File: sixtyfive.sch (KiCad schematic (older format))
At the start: 169 parts, among them J1 Conn_01x12, J2 Conn_ARM_JTAG_SWD_10, Q1 BSS138, SW1 SW_Push, U1 SRV05-4, U2 STM32F072C8Tx, U3 MCP1700-3302E_SOT23

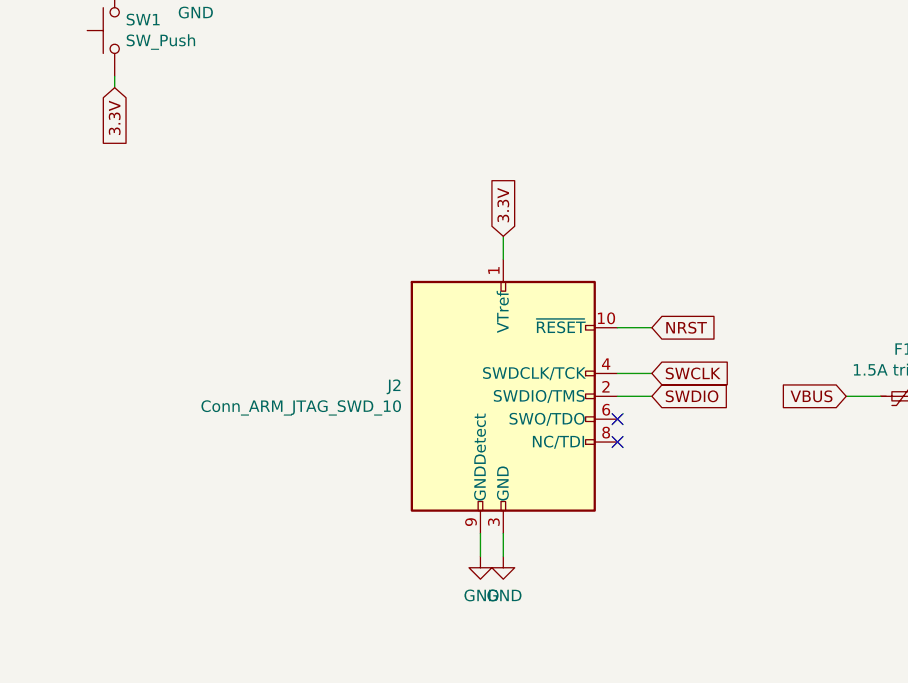
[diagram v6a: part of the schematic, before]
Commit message: Added some decoration, changed the connector and rerouted a tiny bit
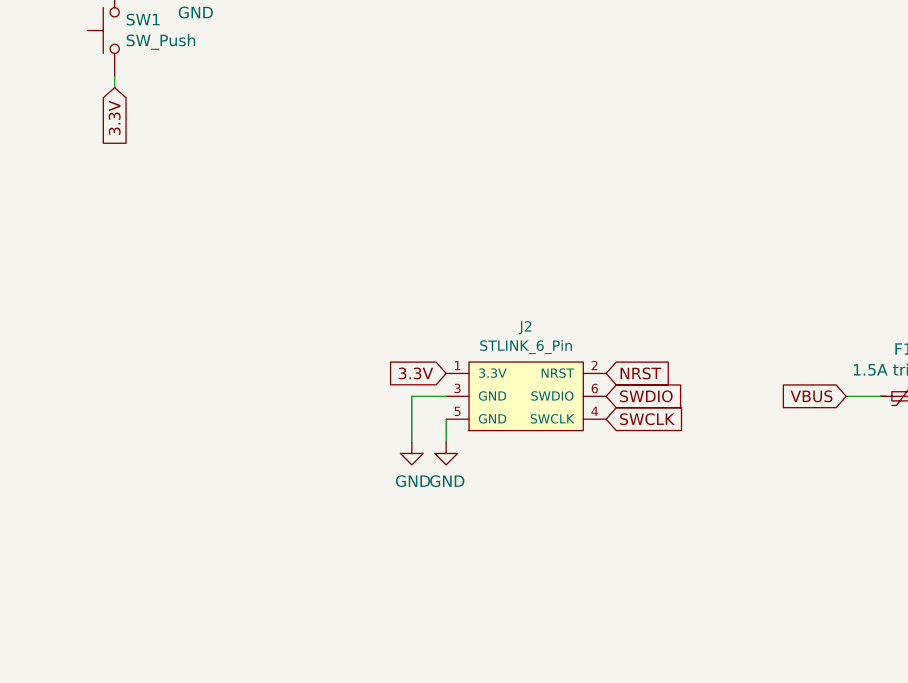
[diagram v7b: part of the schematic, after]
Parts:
- removed J2: Conn_ARM_JTAG_SWD_10, sixtyfive:Conn_ARM_JTAG_SWD_10, symbol Connector:Conn_ARM_JTAG_SWD_10
- added J2: STLINK_6_Pin, 2X3_LOCK, symbol SparkFun-Connectors:STLINK_6_Pin
- DF1: footprint Diode_SMD:D_SOD-123 -> Diode_SMD:D_SMB
- DRGB1, DRGB10, DRGB2, DRGB3, DRGB4, DRGB5, DRGB6, DRGB7, DRGB8, DRGB9: JLCCode (none) -> C114586
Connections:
- net 3.3V: now also J2.1 (3.3V)
- net GND: now also J2.3 (GND), J2.5 (GND)
- net NRST: now also J2.2 (NRST)
- net SWCLK: now also J2.4 (SWCLK)
- net SWDIO: now also J2.6 (SWDIO)
- no-connect marks 6 -> 4
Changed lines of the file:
@@
 Text GLabel 30350 10350 1    50   Input ~ 0
 Col14
-$Comp
-L Connector:Conn_ARM_JTAG_SWD_10 J2
-U 1 1 5F4F806F
-P 22000 20850
-F 0 "J2" H 21557 20896 50  0000 R CNN
-F 1 "Conn_ARM_JTAG_SWD_10" H 21557 20805 50  0000 R CNN
-F 2 "sixtyfive:Conn_ARM_JTAG_SWD_10" H 22000 20850 50  0001 C CNN
-F 3 "http://infocenter.arm.com/help/topic/com.arm.doc.ddi0314h/DDI0314H_coresight_components_trm.pdf" V 21650 19600 50  0001 C CNN
-	1    22000 20850
-	1    0    0    -1
-$EndComp
-Text GLabel 22000 20150 1    50   Input ~ 0
+Text GLabel 21750 20750 0    50   Input ~ 0
 3.3V
-Wire Wire Line
-	22000 20150 22000 20250
 $Comp
 L power:GND #PWR0114
 U 1 1 5F517BF8
-P 21900 21550
-F 0 "#PWR0114" H 21900 21300 50  0001 C CNN
-F 1 "GND" H 21905 21377 50  0000 C CNN
-F 2 "" H 21900 21550 50  0001 C CNN
-F 3 "" H 21900 21550 50  0001 C CNN
-	1    21900 21550
+P 21750 21050
+F 0 "#PWR0114" H 21750 20800 50  0001 C CNN
+F 1 "GND" H 21755 20877 50  0000 C CNN
+F 2 "" H 21750 21050 50  0001 C CNN
+F 3 "" H 21750 21050 50  0001 C CNN
+	1    21750 21050
 	1    0    0    -1
 $EndComp
@@
 L power:GND #PWR0115
 U 1 1 5F519B31
-P 22000 21550
-F 0 "#PWR0115" H 22000 21300 50  0001 C CNN
-F 1 "GND" H 22005 21377 50  0000 C CNN
-F 2 "" H 22000 21550 50  0001 C CNN
-F 3 "" H 22000 21550 50  0001 C CNN
-	1    22000 21550
-	1    0    0    -1
-$EndComp
-Wire Wire Line
-	22000 21550 22000 21450
-Wire Wire Line
-	21900 21450 21900 21550
-Text GLabel 22650 20550 2    50   Input ~ 0
+P 21600 21050
+F 0 "#PWR0115" H 21600 20800 50  0001 C CNN
+F 1 "GND" H 21605 20877 50  0000 C CNN
+F 2 "" H 21600 21050 50  0001 C CNN
+F 3 "" H 21600 21050 50  0001 C CNN
+	1    21600 21050
+	1    0    0    -1
+$EndComp
+Text GLabel 22450 20750 2    50   Input ~ 0
 NRST
-Text GLabel 22650 20750 2    50   Input ~ 0
+Text GLabel 22450 20950 2    50   Input ~ 0
 SWCLK
-Text GLabel 22650 20850 2    50   Input ~ 0
+Text GLabel 22450 20850 2    50   Input ~ 0
 SWDIO
-Wire Wire Line
-	22650 20850 22500 20850
-Wire Wire Line
-	22500 20750 22650 20750
-Wire Wire Line
-	22650 20550 22500 20550
-NoConn ~ 22500 20950
-NoConn ~ 22500 21050
 Text GLabel 29650 18600 2    50   Input ~ 0
 SWDIO
@@
 F 2 "LED_SMD:LED_WS2812B_PLCC4_5.0x5.0mm_P3.2mm" H 11950 18800 50  0001 L TNN
 F 3 "https://cdn-shop.adafruit.com/datasheets/WS2812B.pdf" H 12000 18725 50  0001 L TNN
+F 4 "C114586" H 8300 19100 50  0001 C CNN "JLCCode"
 	1    11900 19100
 	1    0    0    -1
@@
 F 2 "LED_SMD:LED_WS2812B_PLCC4_5.0x5.0mm_P3.2mm" H 12850 18800 50  0001 L TNN
 F 3 "https://cdn-shop.adafruit.com/datasheets/WS2812B.pdf" H 12900 18725 50  0001 L TNN
+F 4 "C114586" H 8300 19100 50  0001 C CNN "JLCCode"
 	1    12800 19100
 	1    0    0    -1
@@
 F 2 "LED_SMD:LED_WS2812B_PLCC4_5.0x5.0mm_P3.2mm" H 13750 18800 50  0001 L TNN
 F 3 "https://cdn-shop.adafruit.com/datasheets/WS2812B.pdf" H 13800 18725 50  0001 L TNN
+F 4 "C114586" H 8300 19100 50  0001 C CNN "JLCCode"
 	1    13700 19100
 	1    0    0    -1
@@
 F 2 "LED_SMD:LED_WS2812B_PLCC4_5.0x5.0mm_P3.2mm" H 14650 18800 50  0001 L TNN
 F 3 "https://cdn-shop.adafruit.com/datasheets/WS2812B.pdf" H 14700 18725 50  0001 L TNN
+F 4 "C114586" H 8300 19100 50  0001 C CNN "JLCCode"
 	1    14600 19100
 	1    0    0    -1
@@
 F 2 "LED_SMD:LED_WS2812B_PLCC4_5.0x5.0mm_P3.2mm" H 8350 18800 50  0001 L TNN
 F 3 "https://cdn-shop.adafruit.com/datasheets/WS2812B.pdf" H 8400 18725 50  0001 L TNN
+F 4 "C114586" H 8300 19100 50  0001 C CNN "JLCCode"
 	1    8300 19100
 	1    0    0    -1
@@
 F 2 "LED_SMD:LED_WS2812B_PLCC4_5.0x5.0mm_P3.2mm" H 9250 18800 50  0001 L TNN
 F 3 "https://cdn-shop.adafruit.com/datasheets/WS2812B.pdf" H 9300 18725 50  0001 L TNN
+F 4 "C114586" H 8300 19100 50  0001 C CNN "JLCCode"
 	1    9200 19100
 	1    0    0    -1
@@
 F 2 "LED_SMD:LED_WS2812B_PLCC4_5.0x5.0mm_P3.2mm" H 10150 18800 50  0001 L TNN
 F 3 "https://cdn-shop.adafruit.com/datasheets/WS2812B.pdf" H 10200 18725 50  0001 L TNN
+F 4 "C114586" H 8300 19100 50  0001 C CNN "JLCCode"
 	1    10100 19100
 	1    0    0    -1
@@
 F 2 "LED_SMD:LED_WS2812B_PLCC4_5.0x5.0mm_P3.2mm" H 11050 18800 50  0001 L TNN
 F 3 "https://cdn-shop.adafruit.com/datasheets/WS2812B.pdf" H 11100 18725 50  0001 L TNN
+F 4 "C114586" H 8300 19100 50  0001 C CNN "JLCCode"
 	1    11000 19100
 	1    0    0    -1
@@
 F 2 "LED_SMD:LED_WS2812B_PLCC4_5.0x5.0mm_P3.2mm" H 15550 18800 50  0001 L TNN
 F 3 "https://cdn-shop.adafruit.com/datasheets/WS2812B.pdf" H 15600 18725 50  0001 L TNN
+F 4 "C114586" H 8300 19100 50  0001 C CNN "JLCCode"
 	1    15500 19100
 	1    0    0    -1
@@
 F 2 "LED_SMD:LED_WS2812B_PLCC4_5.0x5.0mm_P3.2mm" H 16450 18800 50  0001 L TNN
 F 3 "https://cdn-shop.adafruit.com/datasheets/WS2812B.pdf" H 16500 18725 50  0001 L TNN
+F 4 "C114586" H 8300 19100 50  0001 C CNN "JLCCode"
 	1    16400 19100
 	1    0    0    -1
@@
 F 0 "DF1" H 24050 21217 50  0000 C CNN
 F 1 "P6SMB6.8CA" H 24050 21126 50  0000 C CNN
-F 2 "Diode_SMD:D_SOD-123" H 24050 20825 50  0001 C CNN
+F 2 "Diode_SMD:D_SMB" H 24050 20825 50  0001 C CNN
 F 3 "https://datasheet.lcsc.com/szlcsc/Brightking-Elec-TAIWAN-P6SMB6-8CA_C78395.pdf" H 24050 21000 50  0001 C CNN
 F 4 "C78395" H 24050 21000 50  0001 C CNN "JLCCode"
@@
 NoConn ~ 20150 15550
 NoConn ~ 19150 15550
+$Comp
+L SparkFun-Connectors:STLINK_6_Pin J2
+U 1 1 5F74FA48
+P 22100 20850
+F 0 "J2" H 22100 21154 45  0000 C CNN
+F 1 "STLINK_6_Pin" H 22100 21070 45  0000 C CNN
+F 2 "2X3_LOCK" H 22100 21150 20  0001 C CNN
+F 3 "" H 22150 20850 50  0001 C CNN
+	1    22100 20850
+	1    0    0    -1
+$EndComp
+Wire Wire Line
+	21750 20950 21750 21050
+Wire Wire Line
+	21750 20850 21600 20850
+Wire Wire Line
+	21600 20850 21600 21050
 $EndSCHEMATC

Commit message: Reorganized Schematic to be easier to read
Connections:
- net labels added: +3.3V, VBAT, VSS
- net labels removed: Extra13
- wire segments 447 -> 435
- no-connect marks 4 -> 5
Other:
- moved on the sheet: CB1, CB2, CB3, CB4, CB5, CB6, CB7, CB8
